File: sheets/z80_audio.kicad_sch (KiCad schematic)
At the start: 4 parts, among them U22 NEO-D0, U23 HM6116ASP-20, U24 Z80CPU

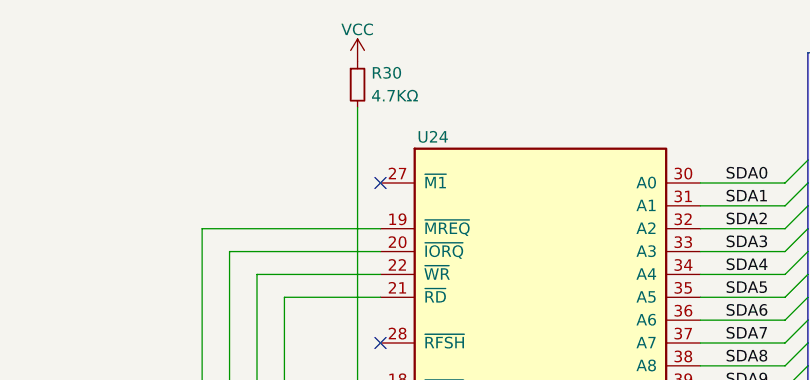
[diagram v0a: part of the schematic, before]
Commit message: More silkscreen tidy up, adding mouser components to BOM
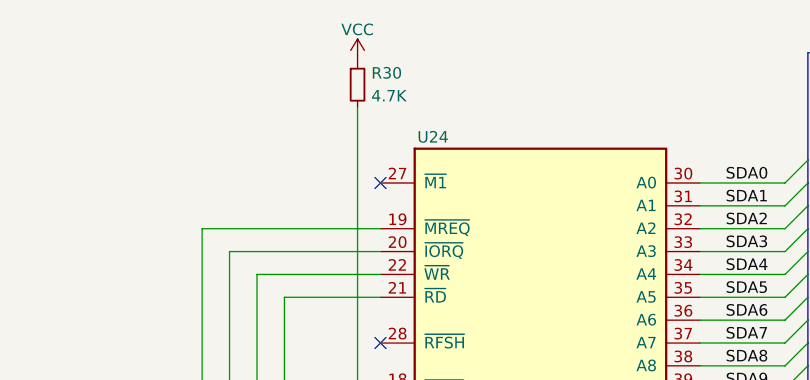
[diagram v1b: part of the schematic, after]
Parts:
- R30: value 4.7KΩ -> 4.7K
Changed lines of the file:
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@@
       (effects (font (size 1.27 1.27)) (justify left))
     )
-    (property "Value" "4.7KΩ" (at 140.208 51.0539 0)
+    (property "Value" "4.7K" (at 140.208 51.0539 0)
       (effects (font (size 1.27 1.27)) (justify left))
     )

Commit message: Little tweaks to silkscreen Updated BOM with mouser parts
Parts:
- R30: Mouser (none) -> 71-RN60D4701F
- U22, U23, U24: Comment (none) -> Use Original
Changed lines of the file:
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@@
     (title "NeoGeo AES 3-5")
     (date "2023-08-27")
-    (rev "BF1.1")
+    (rev "BF1.2")
     (company "SNK")
     (comment 3 "https://github.com/Board-Folk")
@@
       (effects (font (size 1.27 1.27)) hide)
     )
-    (property "Mouser" "" (at 138.684 49.784 0)
+    (property "Mouser" "71-RN60D4701F" (at 138.684 49.784 0)
+      (effects (font (size 1.27 1.27)) hide)
+    )
+    (property "Alternative" "" (at 138.684 49.784 0)
       (effects (font (size 1.27 1.27)) hide)
     )
@@
     )
     (property "Mouser" "" (at 159.004 91.186 0)
+      (effects (font (size 1.27 1.27)) hide)
+    )
+    (property "Alternative" "" (at 159.004 91.186 0)
+      (effects (font (size 1.27 1.27)) hide)
+    )
+    (property "Comment" "Use Original" (at 159.004 91.186 0)
       (effects (font (size 1.27 1.27)) hide)
     )
@@
     )
     (property "Mouser" "" (at 262.636 201.676 0)
+      (effects (font (size 1.27 1.27)) hide)
+    )
+    (property "Comment" "Use Original" (at 262.636 201.676 0)
+      (effects (font (size 1.27 1.27)) hide)
+    )
+    (property "Alternative" "" (at 262.636 201.676 0)
       (effects (font (size 1.27 1.27)) hide)
     )
@@
       (effects (font (size 1.27 1.27)) hide)
     )
+    (property "Alternative" "" (at 258.572 114.046 0)
+      (effects (font (size 1.27 1.27)) hide)
+    )
+    (property "Comment" "Use Original" (at 258.572 114.046 0)
+      (effects (font (size 1.27 1.27)) hide)
+    )

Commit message: update before public
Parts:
- R30: Mouser 71-RN60D4701F -> (none)
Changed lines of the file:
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@@
       (effects (font (size 1.27 1.27)) hide)
     )
-    (property "Mouser" "71-RN60D4701F" (at 138.684 49.784 0)
+    (property "Mouser" "" (at 138.684 49.784 0)
       (effects (font (size 1.27 1.27)) hide)
     )
